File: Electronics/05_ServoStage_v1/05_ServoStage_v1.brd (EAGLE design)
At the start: 100 x 80 mm, 58 parts, among them J1 SCREW_TERMINAL_4, J2 BARRIER_BLOCK-4PIN, J3 CONN_2X3_SMD, U1 XL4005-DEV, U2 XL4005-DEV

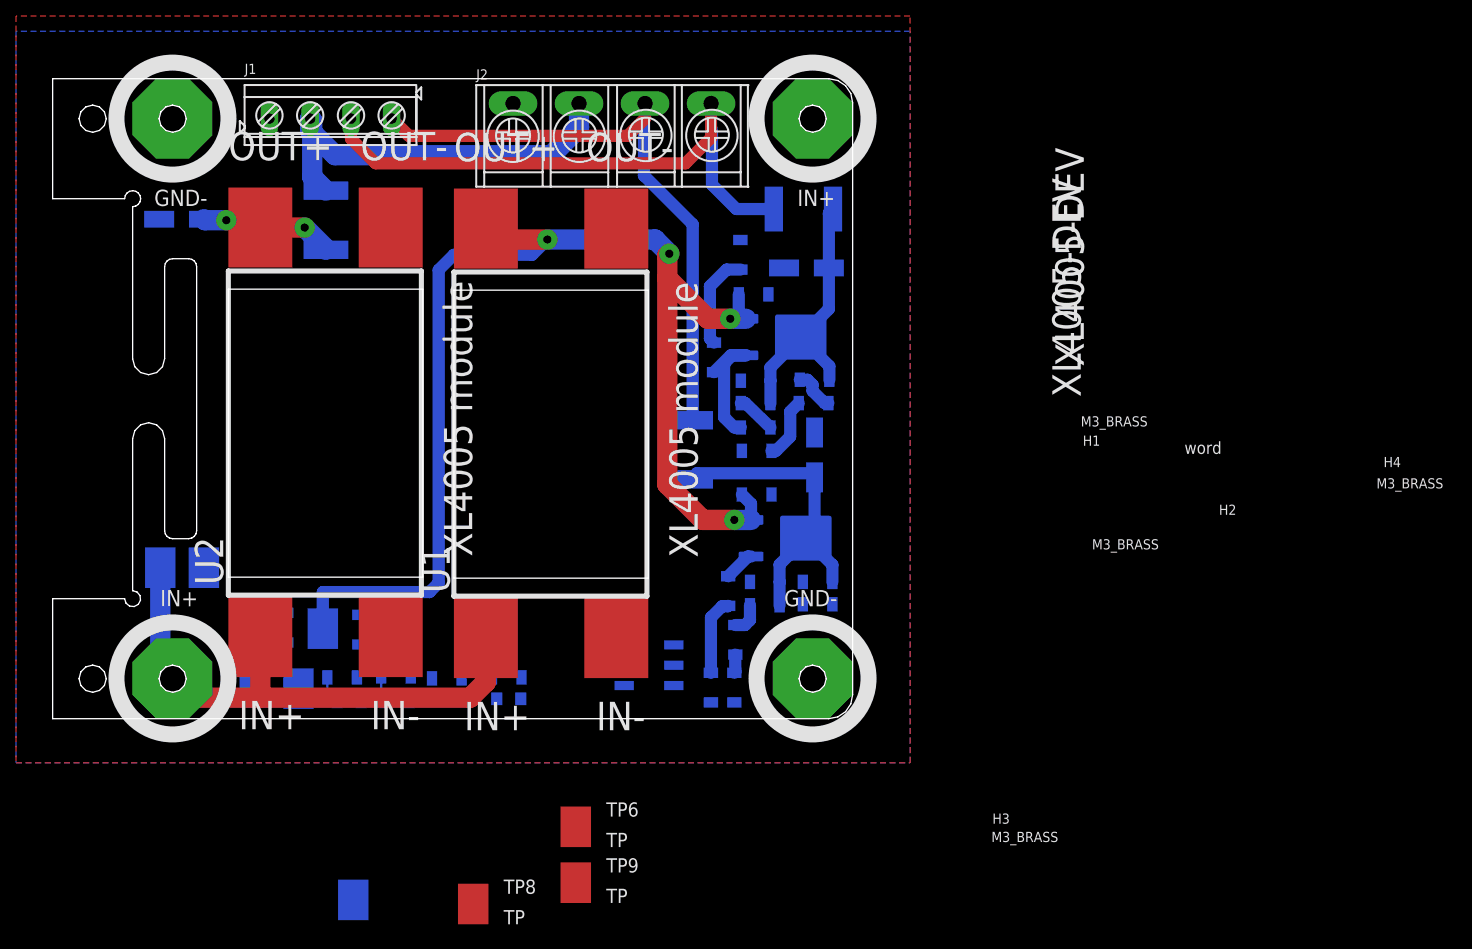
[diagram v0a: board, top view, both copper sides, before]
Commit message: Servo stage: Completed routing
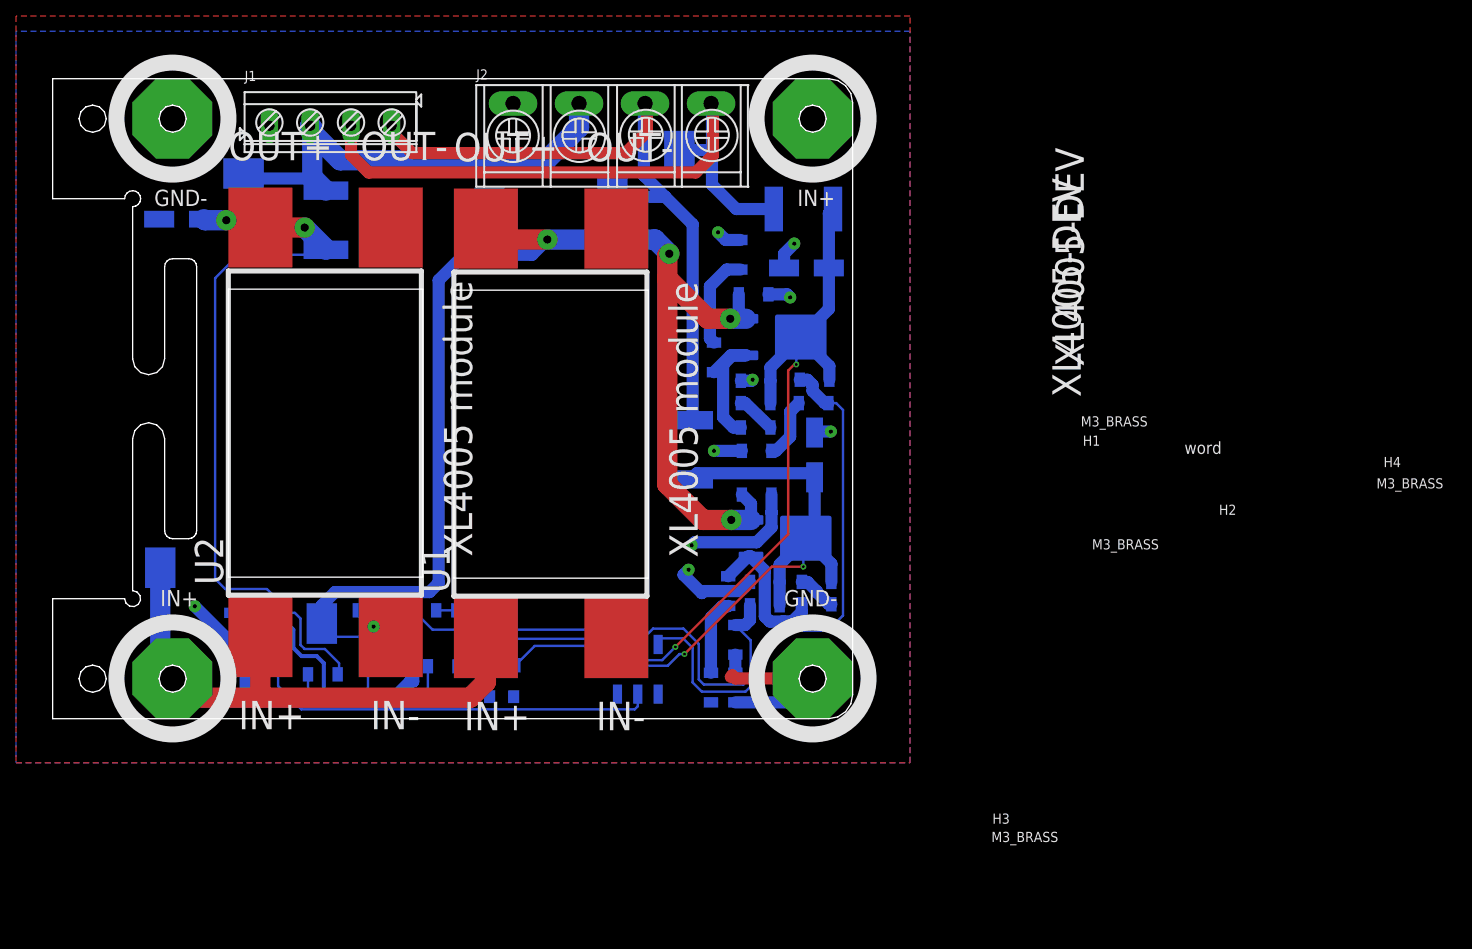
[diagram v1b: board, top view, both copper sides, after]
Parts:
- removed TP6, TP9: TP, Hippo-PS:TP
- moved TP7 102.1 mm to (95.6, 89.2), turned to 0 degrees
- moved TP8 90.1 mm to (87.2, 83.4), flipped to the bottom
- moved TP2 64.6 mm to (71.9, 82.0)
- moved TP5 49.5 mm to (41.1, 86.4), turned to 270 degrees
- moved R13 19.9 mm to (73.3, 24.9)
- moved D1 19.1 mm to (73.4, 21.0)
- moved R26 14.2 mm to (69.6, 31.8), turned to 180 degrees
- moved D7 9.17 mm to (51.2, 21.0)
- moved R12 9.15 mm to (51.1, 23.7)
- moved D2 8.26 mm to (66.0, 21.0), turned to 180 degrees
- moved R23 8.20 mm to (58.5, 25.0)
- moved R22 8.12 mm to (66.0, 24.8)
- moved D3 8.02 mm to (58.5, 21.0), turned to 180 degrees
- moved R25 5.28 mm to (63.4, 31.8), turned to 180 degrees
- moved R24 4.95 mm to (57.3, 31.8), turned to 180 degrees
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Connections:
- net N$17: now also J1.P$4, J2.P$3, TP8.P$1; no longer J1.P$3, J2.P$4
- net N$18: now also J1.P$3, J2.P$4, TP7.P$1; no longer J1.P$4, J2.P$3
- net N$2: now also TP5.P$1
- net NEOPIXELS: no longer TP5.P$1
- net OUT1: no longer TP6.P$1, TP7.P$1
- net OUT2: no longer TP8.P$1, TP9.P$1
- net SIG1: now also J3.3; no longer J3.1
- net SIG2: now also J3.5; no longer J3.2
- net SIG_SMPS: now also J3.1; no longer J3.3
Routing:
- net GND: track 0.00 -> 109.1 mm, vias 0 -> 10
- net NEOPIXELS: track 16.9 -> 94.1 mm
- net OUT2: track 34.3 -> 111.3 mm, vias 0 -> 2
- net SIG2: track 5.23 -> 67.5 mm
- net SIG_NP: track 0.00 -> 56.3 mm
- net OUT1: track 43.4 -> 88.9 mm, vias 0 -> 2
- net SIG_SMPS: track 0.00 -> 30.7 mm
- net N$18: track 51.2 -> 80.6 mm
- net SIG1: track 3.94 -> 32.1 mm
- net N$5: track 3.87 -> 18.5 mm
- net V+: track 161.1 -> 171.8 mm
- net N$2: track 50.6 -> 58.3 mm
- net N$17: track 93.5 -> 87.5 mm
- net N$4: track 0.00 -> 4.93 mm
- net N$7: track 0.00 -> 4.21 mm
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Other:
- board text added: "np"
- board text added: "out2"
- board text removed: "V+"

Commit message: Naming update to Hippo-PD
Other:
- board text added: "hippo-pd servo v1"
- board text removed: "hippo-ps sbc v1"
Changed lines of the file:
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@@
 <text x="88.9" y="91.948" size="1.524" layer="22" font="vector" ratio="20" rot="MR180">out1</text>
 <text x="73.279" y="92.456" size="1.524" layer="22" font="vector" ratio="20" rot="MR180">gnd</text>
-<text x="28.702" y="36.83" size="1.524" layer="22" font="vector" ratio="20" rot="MR90">hippo-ps sbc v1</text>
+<text x="28.702" y="34.798" size="1.524" layer="22" font="vector" ratio="20" rot="MR90">hippo-pd servo v1</text>
 <text x="28.702" y="62.103" size="1.524" layer="22" font="vector" ratio="20" rot="MR90">ek robotgrrl Jul 13, '22</text>
 <text x="81.915" y="92.075" size="1.524" layer="22" font="vector" ratio="20" rot="MR180">np</text>
